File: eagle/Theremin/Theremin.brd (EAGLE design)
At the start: 254 x 101.6 mm, 24 parts, among them Q8 2N3904, U1 LM78L12, U2 LM79L12

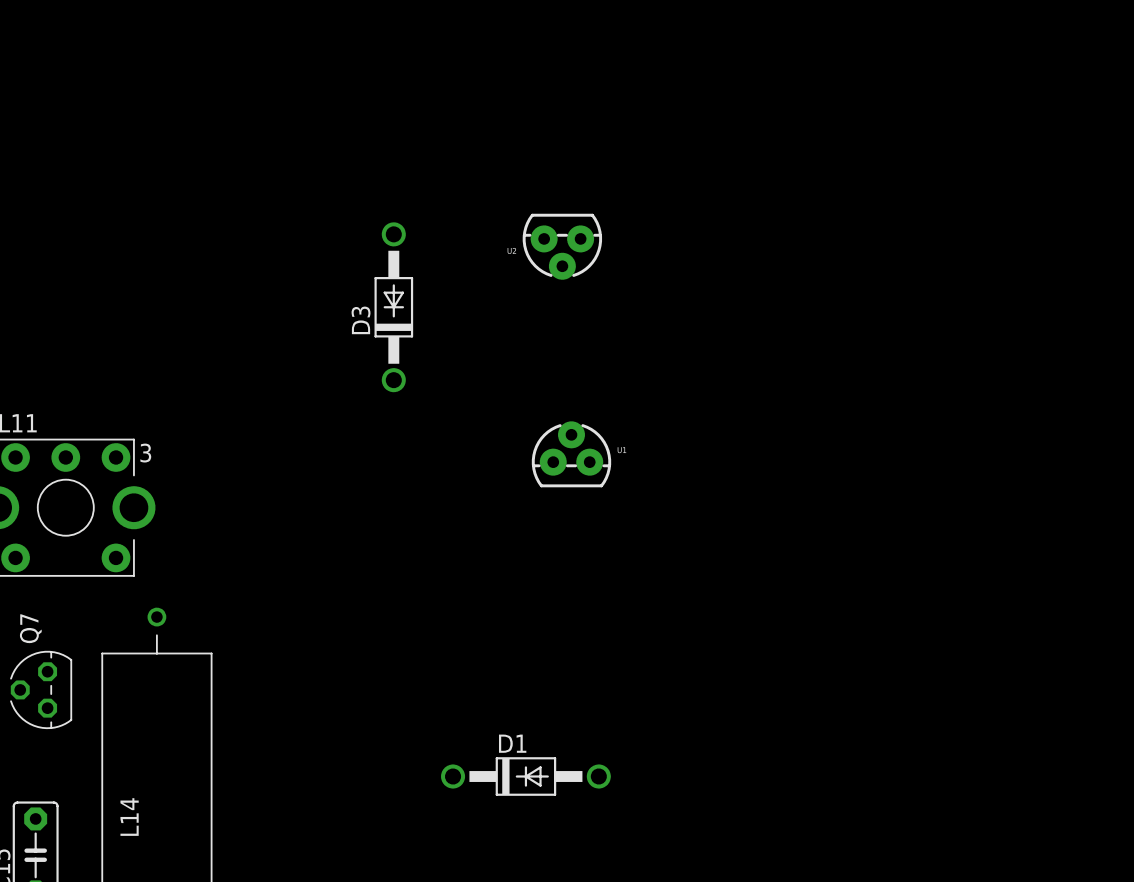
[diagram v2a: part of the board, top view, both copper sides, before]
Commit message: Add big capacitors to theremin power supply
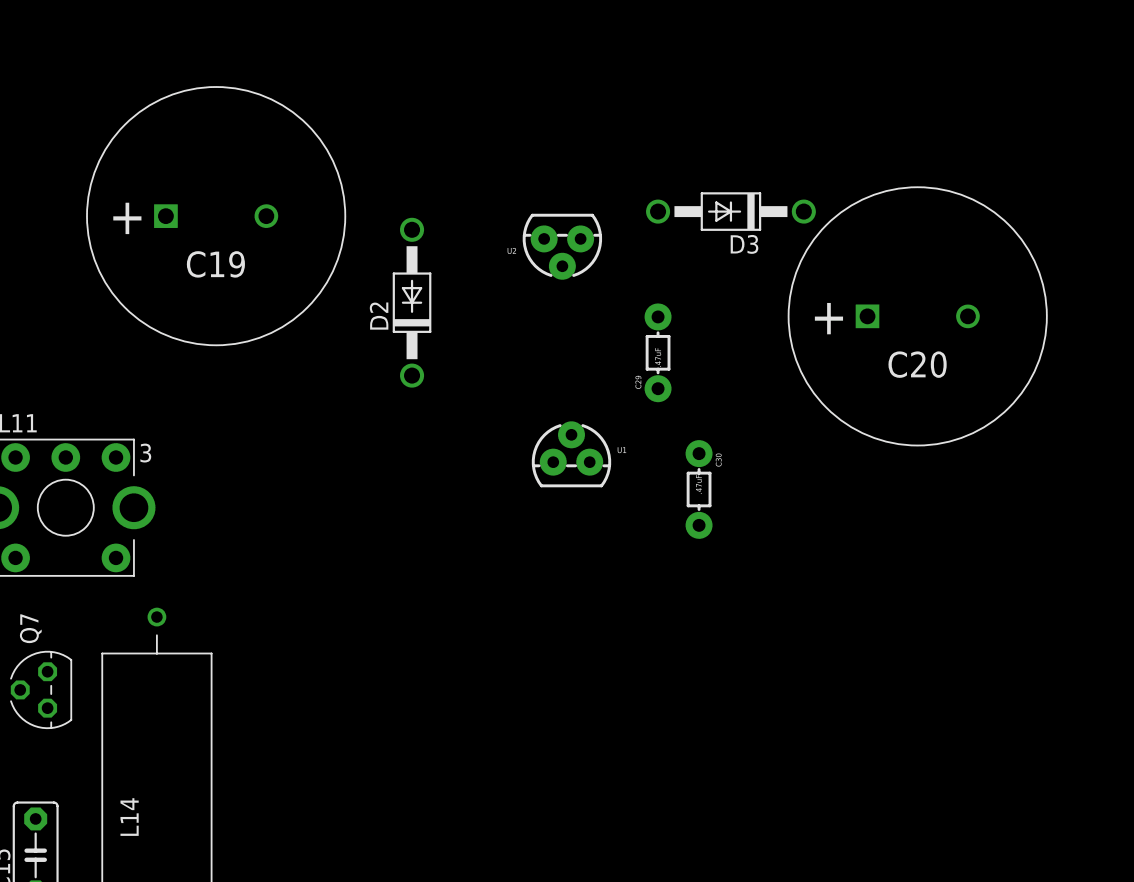
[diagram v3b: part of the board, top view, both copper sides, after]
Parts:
- removed D1: 1N4004, diode:DO41-10
- added C19, C20: 2200uF, marky-parts:10MM-RADIAL-CPOL
- added C29, C30: .47uF, SparkFun-Capacitors:AXIAL-5MM
- added D2: 1N4004, diode:DO41-10
- moved D3 24.4 mm to (84.5, 80.3), turned to 180 degrees
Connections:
- new net N$14: D2.A, D3.C
- net GND: now also C19.P$2, C20.P$1, C29.P$1, C30.P$2
- net N$12: now also C20.P$2, C29.P$2
- net N$13: now also C19.P$1, C30.P$1, D2.C; no longer D1.C
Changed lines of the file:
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@@
 <element name="L14" library="marky-parts" package="FIXED-INDUCTOR-API-DELEVAN" value="22uH" x="44.45" y="38.1"/>
 <element name="C14" library="SparkFun-Capacitors" package="CAP-PTH-LARGE" value="1800pF" x="30.48" y="33.02" rot="R270"/>
-<element name="D3" library="diode" package="DO41-10" value="1N4004" x="60.96" y="73.66" rot="R90"/>
+<element name="D3" library="diode" package="DO41-10" value="1N4004" x="84.455" y="80.3275" rot="R180"/>
 <element name="U2" library="marky-parts" package="TO-92" value="LM79L12" x="72.7075" y="78.4225" rot="R180"/>
 <element name="U1" library="marky-parts" package="TO-92" value="LM78L12" x="73.3425" y="62.865"/>
-<element name="D1" library="diode" package="DO41-10" value="1N4004" x="70.1675" y="40.9575"/>
+<element name="D2" library="diode" package="DO41-10" value="1N4004" x="62.23" y="73.9775" rot="R90"/>
+<element name="C19" library="marky-parts" package="10MM-RADIAL-CPOL" value="2200uF" x="48.5775" y="80.01"/>
+<element name="C20" library="marky-parts" package="10MM-RADIAL-CPOL" value="2200uF" x="97.4725" y="73.025"/>
+<element name="C30" library="SparkFun-Capacitors" package="AXIAL-5MM" value=".47uF" x="82.2325" y="60.96" rot="R270"/>
+<element name="C29" library="SparkFun-Capacitors" package="AXIAL-5MM" value=".47uF" x="79.375" y="70.485" rot="R90"/>
 </elements>
 <signals>
@@
 <contactref element="U2" pad="3"/>
 <contactref element="U1" pad="2"/>
-<wire x1="42.85" y1="59.69" x2="71.4375" y2="78.4225" width="0" layer="19" extent="1-1"/>
+<contactref element="C20" pad="P$1"/>
+<contactref element="C19" pad="P$2"/>
+<contactref element="C29" pad="P$1"/>
+<contactref element="C30" pad="P$2"/>
+<wire x1="71.4375" y1="78.4225" x2="93.9725" y2="73.025" width="0" layer="19" extent="1-1"/>
+<wire x1="73.3425" y1="64.77" x2="71.4375" y2="78.4225" width="0" layer="19" extent="1-1"/>
+<wire x1="52.0775" y1="80.01" x2="71.4375" y2="78.4225" width="0" layer="19" extent="1-1"/>
+<wire x1="42.85" y1="59.69" x2="52.0775" y2="80.01" width="0" layer="19" extent="1-1"/>
 <wire x1="33.35" y1="59.69" x2="42.85" y2="59.69" width="0" layer="19" extent="1-1"/>
 <wire x1="20.32" y1="58.42" x2="33.35" y2="59.69" width="0" layer="19" extent="1-1"/>
@@
 <wire x1="30.48" y1="24.13" x2="17.78" y2="19.05" width="0" layer="19" extent="1-1"/>
 <wire x1="36" y1="38" x2="30.48" y2="24.13" width="0" layer="19" extent="1-1"/>
-<wire x1="73.3425" y1="64.77" x2="17.78" y2="19.05" width="0" layer="19" extent="1-1"/>
+<wire x1="82.2325" y1="58.46" x2="17.78" y2="19.05" width="0" layer="19" extent="1-1"/>
+<wire x1="79.375" y1="67.985" x2="82.2325" y2="58.46" width="0" layer="19" extent="1-1"/>
 </signal>
 <signal name="N$7">
@@
 <contactref element="U2" pad="2"/>
 <contactref element="D3" pad="A"/>
-<wire x1="72.7075" y1="76.5175" x2="60.96" y2="78.74" width="0" layer="19" extent="1-1"/>
+<contactref element="C20" pad="P$2"/>
+<contactref element="C29" pad="P$2"/>
+<wire x1="72.7075" y1="76.5175" x2="100.9725" y2="73.025" width="0" layer="19" extent="1-1"/>
+<wire x1="79.375" y1="80.3275" x2="72.7075" y2="76.5175" width="0" layer="19" extent="1-1"/>
+<wire x1="79.375" y1="72.985" x2="79.375" y2="80.3275" width="0" layer="19" extent="1-1"/>
 </signal>
 <signal name="N$13">
-<contactref element="D1" pad="C"/>
+<contactref element="D2" pad="C"/>
 <contactref element="U1" pad="1"/>
-<wire x1="72.0725" y1="62.865" x2="65.0875" y2="40.9575" width="0" layer="19" extent="1-1"/>
+<contactref element="C19" pad="P$1"/>
+<contactref element="C30" pad="P$1"/>
+<wire x1="62.23" y1="68.8975" x2="72.0725" y2="62.865" width="0" layer="19" extent="1-1"/>
+<wire x1="45.0775" y1="80.01" x2="72.0725" y2="62.865" width="0" layer="19" extent="1-1"/>
+<wire x1="82.2325" y1="63.46" x2="62.23" y2="68.8975" width="0" layer="19" extent="1-1"/>
+</signal>
+<signal name="N$14">
+<contactref element="D3" pad="C"/>
+<contactref element="D2" pad="A"/>
+<wire x1="62.23" y1="79.0575" x2="89.535" y2="80.3275" width="0" layer="19" extent="1-1"/>
 </signal>
 </signals>

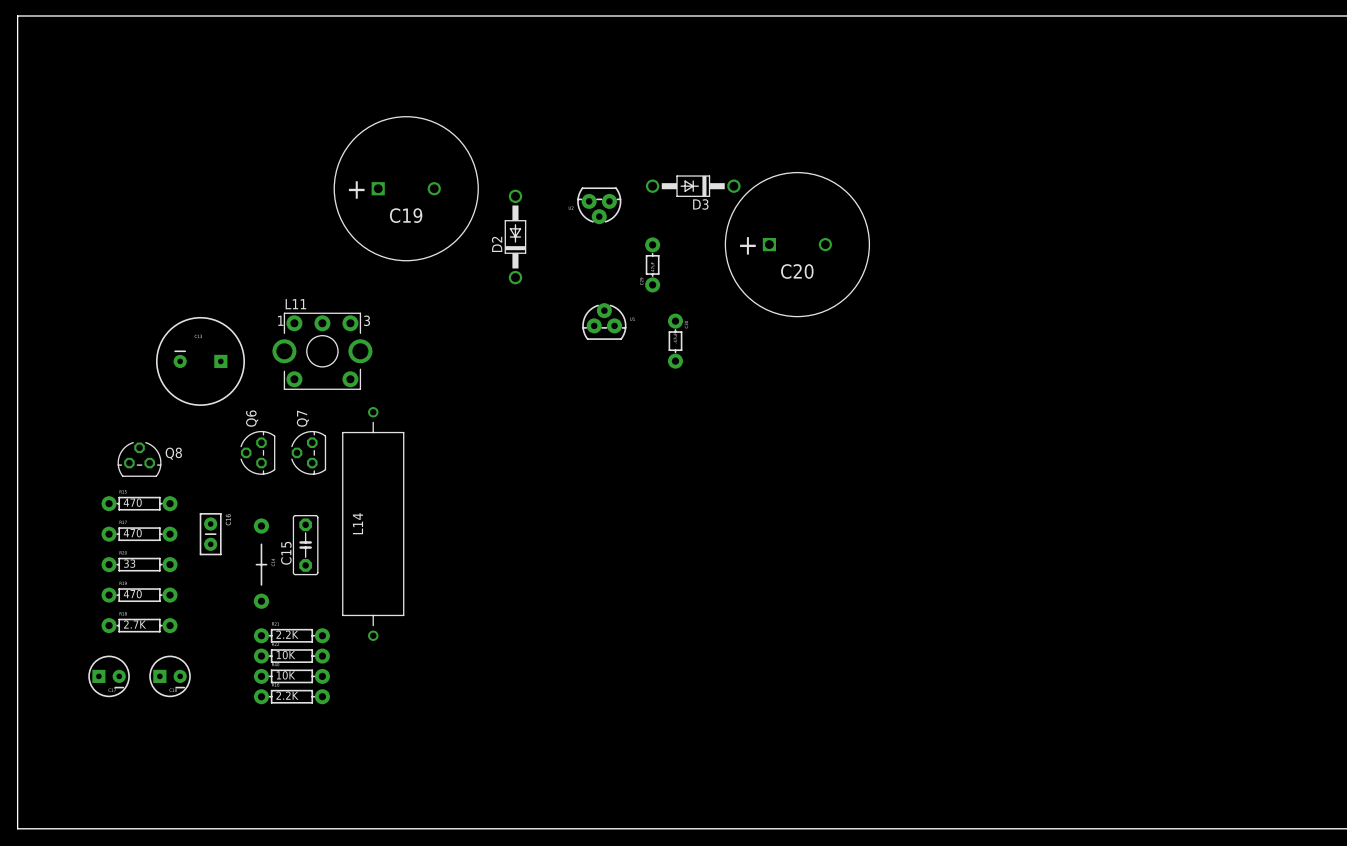
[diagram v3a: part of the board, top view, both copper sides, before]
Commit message: Added Variable Pitch Oscillator cleaned up layout of schematic
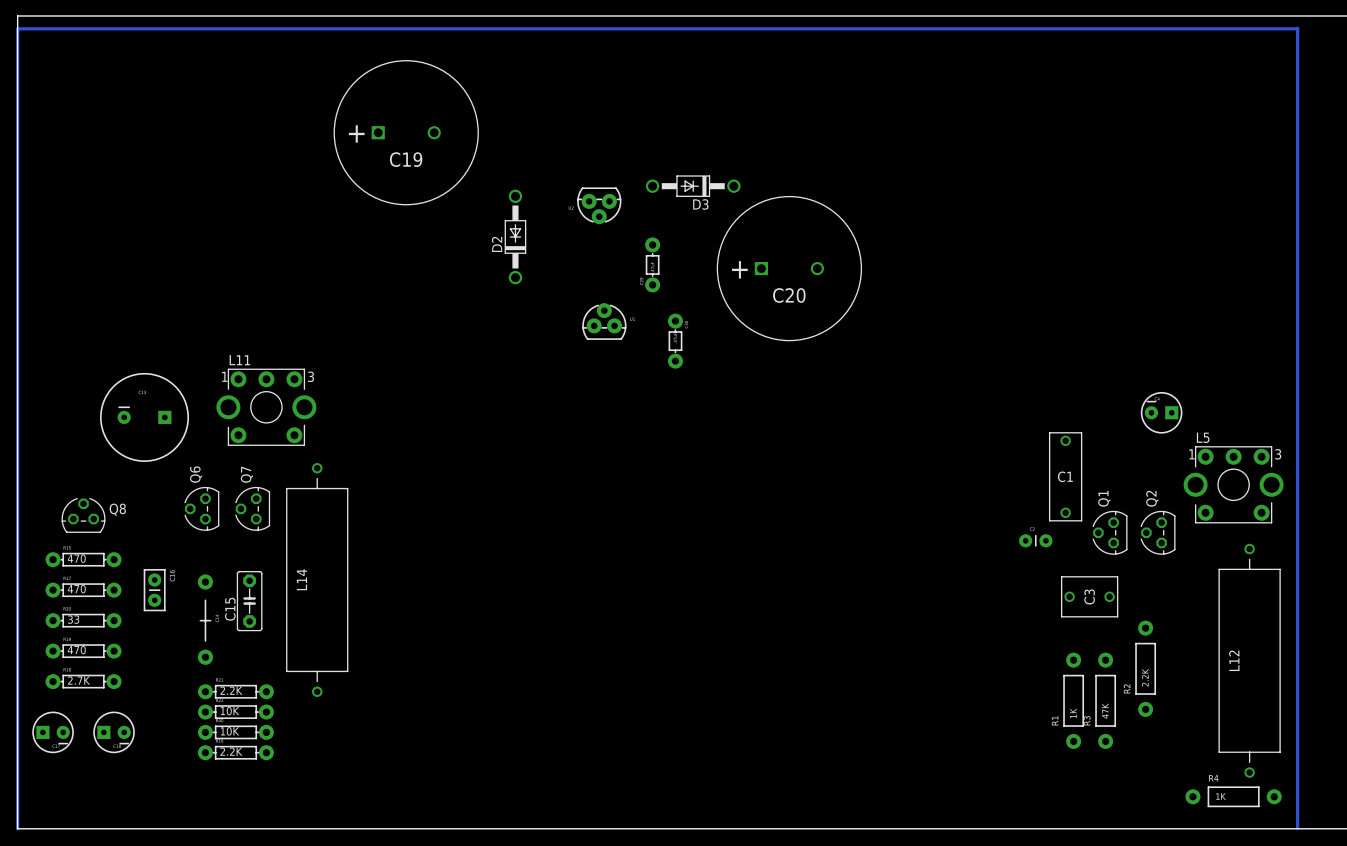
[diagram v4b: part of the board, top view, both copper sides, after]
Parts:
- added C1: 3300pF, marky-parts:9M-CAP-RADIAL
- added C2: 15pF, SparkFun-Capacitors:CAP-PTH-SMALL
- added C3: 0.01uF, marky-parts:5M-CAP-RADIAL
- added C4: 1uF, SparkFun-Passives:CPOL-RADIAL-10UF-25V
- added L12: 47uH, marky-parts:FIXED-INDUCTOR-API-DELEVAN
- added L5: 47uH, marky-parts:SLOT-TEN
- added Q1, Q2: (no value), transistor:TO92
- added R1, R4: 1K, SparkFun-Resistors:AXIAL-0.4
- added R2: 2.2K, SparkFun-Resistors:AXIAL-0.4
- added R3: 47K, SparkFun-Resistors:AXIAL-0.4
- moved C14 9.90 mm to (23.5, 26.0)
- moved R16 9.90 mm to (27.3, 9.51)
- moved R20 9.90 mm to (8.24, 26.0)
- moved C13 9.90 mm to (15.9, 51.4)
- moved C15 9.90 mm to (29.0, 28.5)
- moved C16 9.90 mm to (17.1, 31.1)
- moved C17 9.90 mm to (4.43, 12.1)
- moved C18 9.90 mm to (12.1, 12.1)
- moved L11 9.90 mm to (31.1, 52.7)
- moved L14 9.90 mm to (37.5, 31.1)
- moved Q6 9.90 mm to (23.5, 40.0)
- moved Q7 9.90 mm to (29.8, 40.0)
- moved Q8 9.90 mm to (8.24, 38.7)
- moved R15 9.90 mm to (8.24, 33.6)
- moved R17 9.90 mm to (8.24, 29.8)
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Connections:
- new net 5V: C1.P$1, C13.1, C3.P$2, C4.1, L11.IN$1, L5.IN$1, Q2.1, Q7.1, R3.P$2
- new net N$16: Q1.2, R1.P$2
- new net N$17: C1.P$2, C2.1, C3.P$1, L12.P$2, Q1.1
- new net N$18: Q1.3, Q2.3, R2.P$2
- new net N$19: Q2.2, R3.P$1, R4.P$1
- new net N$20: C2.2
- net -12V: now also R2.P$1
- net GND: now also C4.2, L5.TAB@7, L5.TAB@8, R1.P$1, R4.P$2
- net N$10: now also L12.P$1, L5.OUT$3; no longer C13.1, L11.IN$1, Q7.1
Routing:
- net N$15: track 0.00 -> 360.0 mm
